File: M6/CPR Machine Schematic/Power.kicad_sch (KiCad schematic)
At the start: 8 parts, among them J1 Battery EC2 Socket, K1 Contactor - NO, SW1 SW_SPST, U4 TSR_1-24120, U5 TSR_1-2450, U6 TSR_1-2433

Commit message: ToF
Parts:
- K1: value Contactor - NO -> Contactor - Norm. Open
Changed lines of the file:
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@@
 			)
 		)
-		(property "Value" "Contactor - NO"
+		(property "Value" "Contactor - Norm. Open"
 			(at 99.06 40.64 90)
 			(effects

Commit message: morer kicad
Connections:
- net +22.2V: now also K1.13; no longer F1.2
- net at F1.1: now also J1.1 (Pin_1), U4.1 (Vin); no longer K1.13
- new net: F1.2, K1.14
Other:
- moved on the sheet: F1, U5, U6

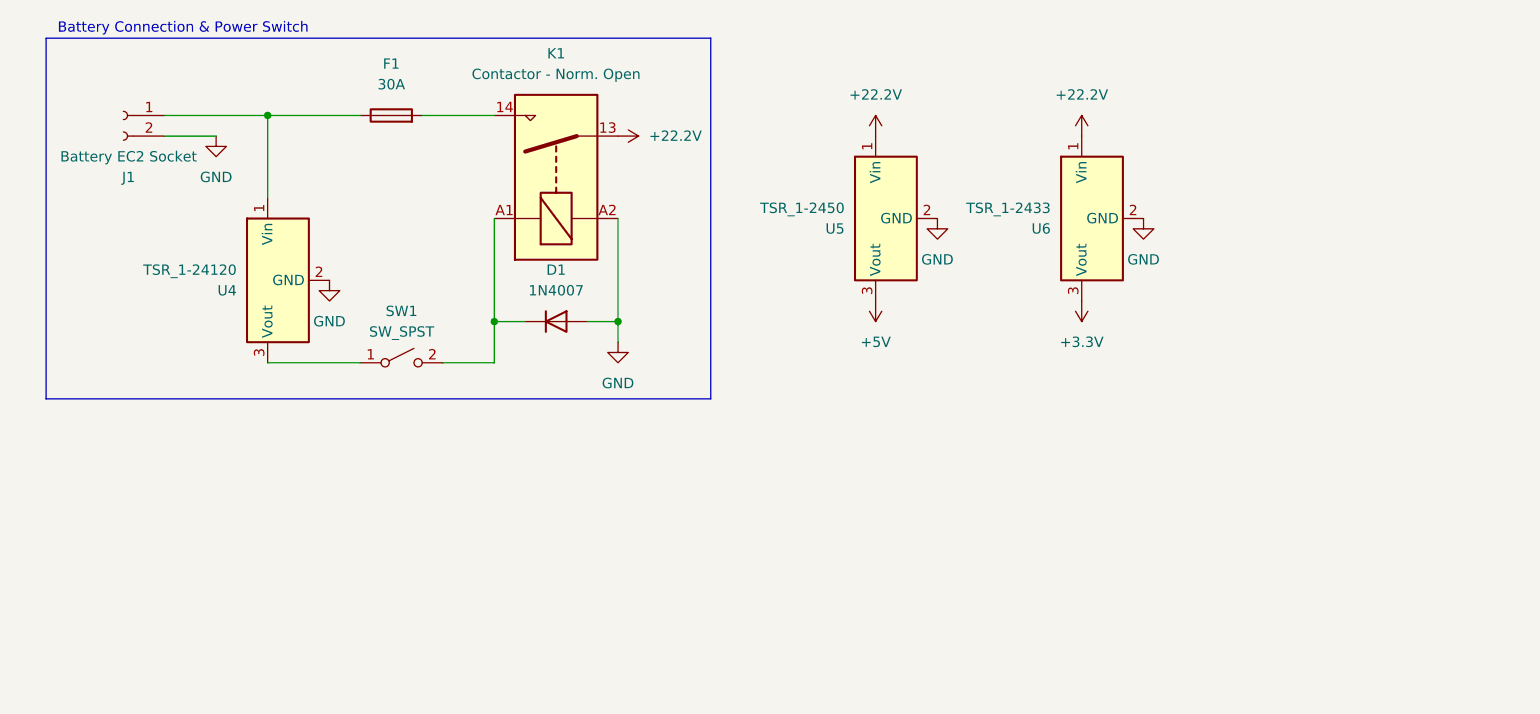
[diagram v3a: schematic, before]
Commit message: Single-pager KiCAD
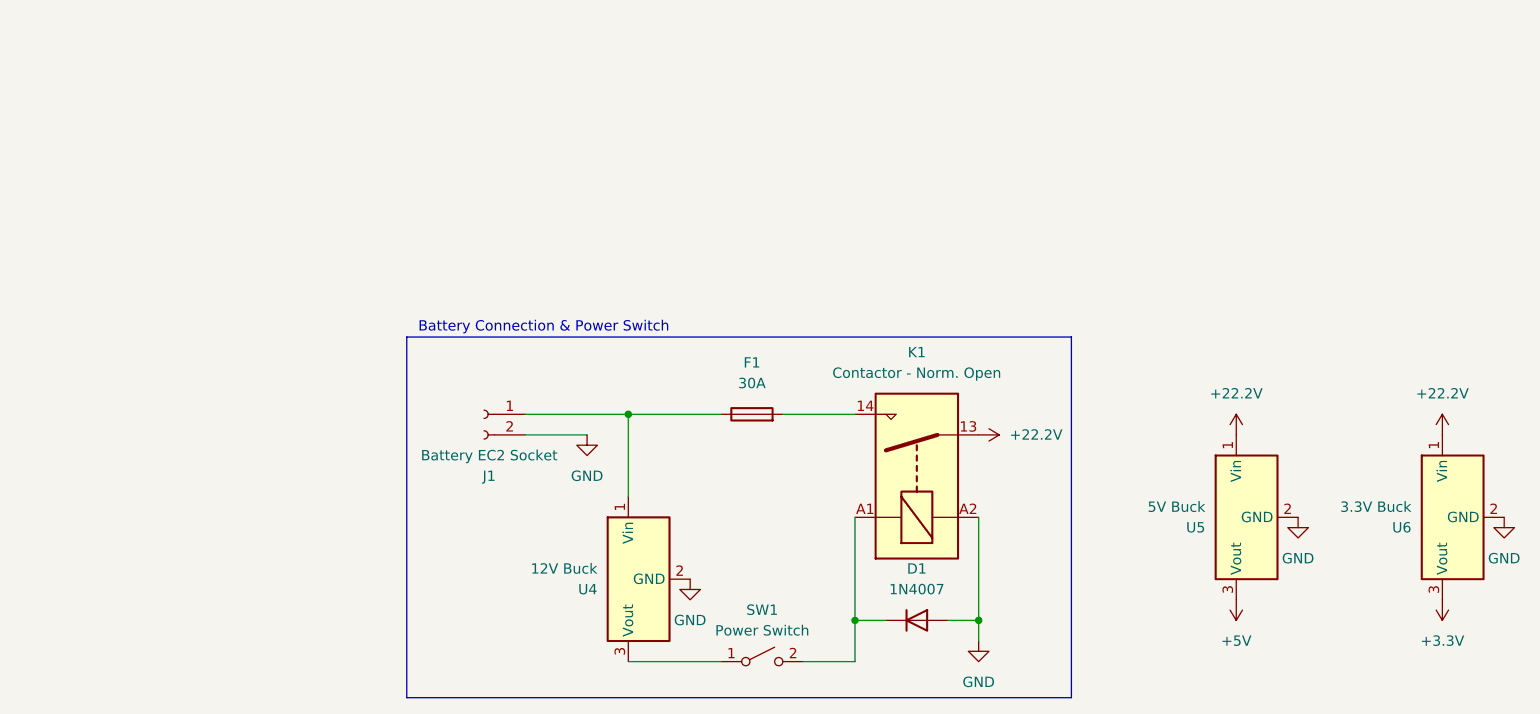
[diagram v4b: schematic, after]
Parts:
- SW1: value SW_SPST -> Power Switch
- U4: value TSR_1-24120 -> 12V Buck
- U5: value TSR_1-2450 -> 5V Buck
- U6: value TSR_1-2433 -> 3.3V Buck
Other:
- moved on the sheet: D1, F1, J1, K1, SW1, U4, U5, U6

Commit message: Start of Schematic V2
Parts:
- removed U5: 5V Buck, Converter_DCDC:Converter_DCDC_TRACO_TSR-1_THT, symbol Regulator_Switching:TSR_1-2450
- added C1, C5, C7: 0.1 uF, symbol Device:C
- added C10: 0.18 uF, symbol Device:C
- added C11: 330 pF, symbol Device:C
- added C12: 15 nF, symbol Device:C
- added C2: 50 uF, symbol Device:C
- added C3: 22 pF, symbol Device:C
- added C4, C6, C8, C9: 2.2 uF, symbol Device:C
- added D2: B220, Diode_SMD:D_SMB, symbol Diode:B220
- added D3: SS24, Diode_SMD:D_SMA, symbol Diode:SS24
- added J2: Conn_01x05_Pin, symbol Connector:Conn_01x05_Pin
- added J4: Conn_01x03_Pin, symbol Connector:Conn_01x03_Pin
- added J5, J6: Conn_01x02_Pin, symbol Connector:Conn_01x02_Pin
- added J7: Conn_01x12_Pin, symbol Connector:Conn_01x12_Pin
- added L1: 12 uH, symbol Device:L
- added L2: 5 uH, symbol Device:L
- added LED1, LED2, LED3, LED4: Green, LED_LTST-C170GKT_LTO, symbol Custom_Parts:LTST-C170GKT
- added Q1: 2N3904, Package_TO_SOT_THT:TO-92_Inline, symbol Transistor_BJT:2N3904
- added R1, R4: 50 kOhm, symbol Device:R_US
- added R10: 660 Ohm, symbol Device:R_US
- added R11: 193 Ohm, symbol Device:R_US
- added R12: 80 Ohm, symbol Device:R_US
- added R2: 3.57 kOhm, symbol Device:R_US
- added R3: 20 kOhm, symbol Device:R_US
- added R7: 2 kOhm, symbol Device:R_US
- added R8: 47 kOhm, symbol Device:R_US
- added R9: 1.4 kOhm, symbol Device:R_US
- added TP1: Battery, symbol Connector:TestPoint
- added TP2: 12 V, symbol Connector:TestPoint
- added TP3: 5 V, symbol Connector:TestPoint
- added TP4: 3V3, symbol Connector:TestPoint
- added U1: LT1765EFE-5_PBF, LT1765EFE-5_PBF:SOP65P640X110-17N, symbol Custom_Parts:LT1765EFE-5_PBF
- added U2: MAX42402AFLB+, 21-100701_90-100241_ADI, symbol Custom_Parts:MAX42402AFLB+
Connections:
- net +22.2V: now also C4.2, C5.2, J6.1 (Pin_1), J6.2 (Pin_2), R9.2, TP1.1, U2.1 (EN), U2.3 (SUP)
- net +3.3V: now also J4.1 (Pin_1), J4.2 (Pin_2), J4.3 (Pin_3), R12.2, TP4.1
- net +5V: now also C12.1, D3.2 (A), J2.1 (Pin_1), J2.2 (Pin_2), J2.3 (Pin_3), J2.4 (Pin_4), J2.5 (Pin_5), L2.1, R11.2, R3.2, TP3.1, U1.12 (FB)
- net GND: now also C11.1, C2.2, C4.1, C5.1, C6.1, C7.1, C9.1, D2.2 (A), J7.1 (Pin_1), J7.10 (Pin_10), J7.11 (Pin_11), J7.12 (Pin_12), J7.2 (Pin_2), J7.3 (Pin_3), J7.4 (Pin_4), J7.5 (Pin_5), J7.6 (Pin_6), J7.7 (Pin_7), J7.8 (Pin_8), J7.9 (Pin_9), LED1.1, LED2.1, LED3.1, LED4.1, Q1.1 (E), R2.2, R8.1, U1.1 (GND_3), U1.14 (SYNC), U1.16 (GND), U1.17 (EP), U1.8 (GND_4), U1.9 (GND_2), U2.10 (PGND), U2.8 (PGND)
- new net: C11.2, Q1.3 (C), U1.13 (VC)
- new net: C12.2, R7.1
- new net: C1.1, L1.2, U2.9 (LX)
- new net: LED3.2, R11.1
- new net: Q1.2 (B), R7.2, R8.2
- new net: R3.1, U2.17 (PGOOD)
- new net: C3.1, R1.2, R2.1, U2.16 (SPS)
- new net: C10.1, D2.1 (K), L2.2, U1.5 (SW_2), U1.6 (SW)
- new net: C10.2, D3.1 (K), U1.2 (BOOST)
- new net: R4.1, U1.11 (~SHDN)
- new net: LED1.2, R9.1
- new net: C1.2, U2.13 (BST)
- new net: LED4.2, R12.1
- new net: C6.2, C7.2, U2.11 (SUP)
- new net: C8.1, U2.14 (GND)
- new net: C8.2, U2.15 (BIAS), U2.16 (SPS), U2.17 (PGOOD)
- new net: LED2.2, R10.1
- new net +12V: C2.1, C3.2, C9.2, J5.1 (Pin_1), J5.2 (Pin_2), L1.1, R1.1, R10.2, R4.2, TP2.1, U1.3 (VIN_2), U1.4 (VIN)
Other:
- note added: "12V - 5V Regulator"
- note added: "Batt - 12V Regulator"
- note added: "Placeholder 12V-3V Converter"
- note added: "Power Status LEDs"
- note added: "Spare Header Pins"
- note added: "Test Points"
- moved on the sheet: D1, F1, J1, K1, SW1, U4, U6

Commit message: More PCB Progress
All Footprints
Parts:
- removed D1: 1N4007, Diode_THT:D_DO-41_SOD81_P10.16mm_Horizontal, symbol Diode:1N4007
- removed F1: 30A, symbol Device:Fuse
- removed K1: Contactor - Norm. Open, symbol Relay:Relay_SPST-NO
- removed SW1: Power Switch, symbol Switch:SW_SPST
- added J3: Power Switch, TerminalBlock:TerminalBlock_MaiXu_MX126-5.0-02P_1x02_P5.00mm, symbol Connector:Conn_01x02_Socket
- C1, C10, C11, C12, C2, C3, C4, C5, C6, C7, C8, C9: footprint (none) -> Capacitor_SMD:C_1206_3216Metric
- J1: value Battery EC2 Socket -> Contactor 22.2V IN; footprint (none) -> TerminalBlock:TerminalBlock_MaiXu_MX126-5.0-02P_1x02_P5.00mm
- J2: value Conn_01x05_Pin -> 5V Spare Headers; footprint (none) -> Connector_PinHeader_2.54mm:PinHeader_1x05_P2.54mm_Vertical
- J4: value Conn_01x03_Pin -> 3V3 Spare Headers; footprint (none) -> Connector_PinHeader_2.54mm:PinHeader_1x03_P2.54mm_Vertical
- J5: value Conn_01x02_Pin -> 12 Spare headers; footprint (none) -> Connector_PinHeader_2.54mm:PinHeader_1x02_P2.54mm_Vertical
- J6: value Conn_01x02_Pin -> Battery Spare headers; footprint (none) -> Connector_PinHeader_2.54mm:PinHeader_1x02_P2.54mm_Vertical
- J7: value Conn_01x12_Pin -> GND Spare Headers; footprint (none) -> Connector_PinHeader_2.54mm:PinHeader_1x12_P2.54mm_Vertical
- L1: footprint (none) -> DR124_120_R:IND_CB_DR124
- L2: footprint (none) -> SRU8043_6R8Y:IND_BOURNS_SRU8043
- LED1, LED2, LED3, LED4: footprint LED_LTST-C170GKT_LTO -> LTST_C170GKT:LED_LTST-C170GKT_LTO
- R1, R10, R11, R12, R2, R3, R4, R7, R8, R9: footprint (none) -> Resistor_SMD:R_1206_3216Metric
- TP1: footprint (none) -> TestPoint:TestPoint_THTPad_4.0x4.0mm_Drill2.0mm
- TP2, TP3, TP4: footprint (none) -> TestPoint:TestPoint_THTPad_D4.0mm_Drill2.0mm
- U1: footprint LT1765EFE-5_PBF:SOP65P640X110-17N -> LT1765EFE_5_PBF:SOP65P640X110-17N
- U2: footprint 21-100701_90-100241_ADI -> MAX42402AFLB_:21-100701_90-100241_ADI
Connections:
- net +12V: now also U6.1 (Vin)
- net +22.2V: now also J1.1 (Pin_1); no longer U6.1 (Vin)
- net +5V: no longer R3.2
- net at U4.1 (Vin): now also J3.1 (Pin_1); no longer J1.1 (Pin_1)
- net at U4.3 (Vout): now also J3.2 (Pin_2)
- net at C8.2, U2.15 (BIAS), U2.16 (SPS)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: now also R3.2
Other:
- note added: "From Switch"
- note added: "To Contactor"
- moved on the sheet: J1, U4

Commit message: finished PCB Draft
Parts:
- added F1: 5A, Fuse:Fuse_1206_3216Metric, symbol Device:Fuse
- added Q2: AO3407A, Package_TO_SOT_SMD:SOT-23-3, symbol 2679:DMG2305UX-13 MOSFET
- added Q4: DMMT5401 PNP, 2679:SOT95P285X140-6N, symbol 2679:DMMT5401 PNP
- added R13: 10 kOhm, Resistor_SMD:R_1206_3216Metric, symbol Device:R_US
- added R14: 47 kOhm, Resistor_SMD:R_1206_3216Metric, symbol Device:R_US
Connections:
- net +22.2V: now also F1.2; no longer J1.1 (Pin_1)
- net GND: now also C8.1, U2.4 (PGND), U2.6 (PGND), R13.2, R14.2; no longer U2.8 (PGND)
- net at C1.1, L1.2: now also U2.5 (LX); no longer U2.9 (LX)
- net From Switch: now reaches U4.1 (Vin)
- net From Switch: now also J3.2 (Pin_2); no longer J3.1 (Pin_1)
- net To Contactor: now reaches U4.3 (Vout)
- net To Contactor: now also J3.1 (Pin_1); no longer J3.2 (Pin_2)
- net at R3.1: now also U2.14 (PGOOD); no longer U2.17 (PGOOD)
- net at C8.2, R3.2, U2.15 (SYNC): now also U2.11 (BIAS), U2.12 (SPS); no longer U2.16 (SPS), U2.17 (PGOOD)
- net at C3.1, R1.2, R2.1: now also U2.13 (FB); no longer U2.16 (SPS)
- net at C1.2: now also U2.9 (BST); no longer U2.13 (BST)
- net at C6.2, C7.2: now also U2.7 (SUP); no longer U2.11 (SUP)
- new net: Q4.1, Q4.2, Q4.3, R13.1
- new net: Q2.1, Q4.4, R14.1
- new net: F1.1, Q2.2, Q4.5
- new net Contactor +: J1.1 (Pin_1), Q2.3, Q4.6
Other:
- note added: "0V Diode"
- note removed: "From Switch"
- note removed: "To Contactor"
- moved on the sheet: J1, J3, U4

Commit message: PCB Feedback V1
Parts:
- R11: value 193 Ohm -> 220 Ohm
- R12: value 80 Ohm -> 100 Ohm
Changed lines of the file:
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@@
 			)
 		)
-		(property "Value" "193 Ohm"
+		(property "Value" "220 Ohm"
 			(at 195.834 50.546 0)
 			(effects
@@
 			)
 		)
-		(property "Value" "80 Ohm"
-			(at 207.518 50.546 0)
+		(property "Value" "100 Ohm"
+			(at 208.534 50.546 0)
 			(effects
 				(font
